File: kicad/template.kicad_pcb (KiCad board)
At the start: 2 copper layers, 84.1 x 61.7 mm, 7 parts, among them J1 Bus_PCI_Express_x1, J6 USB_C_Receptacle_USB2.0_16P, U1 MCP25625T-E/ML, U2 RP2040, U4 W25Q128JVP, X1 ABM8-272-T3, Y1 X322516MLB4SI

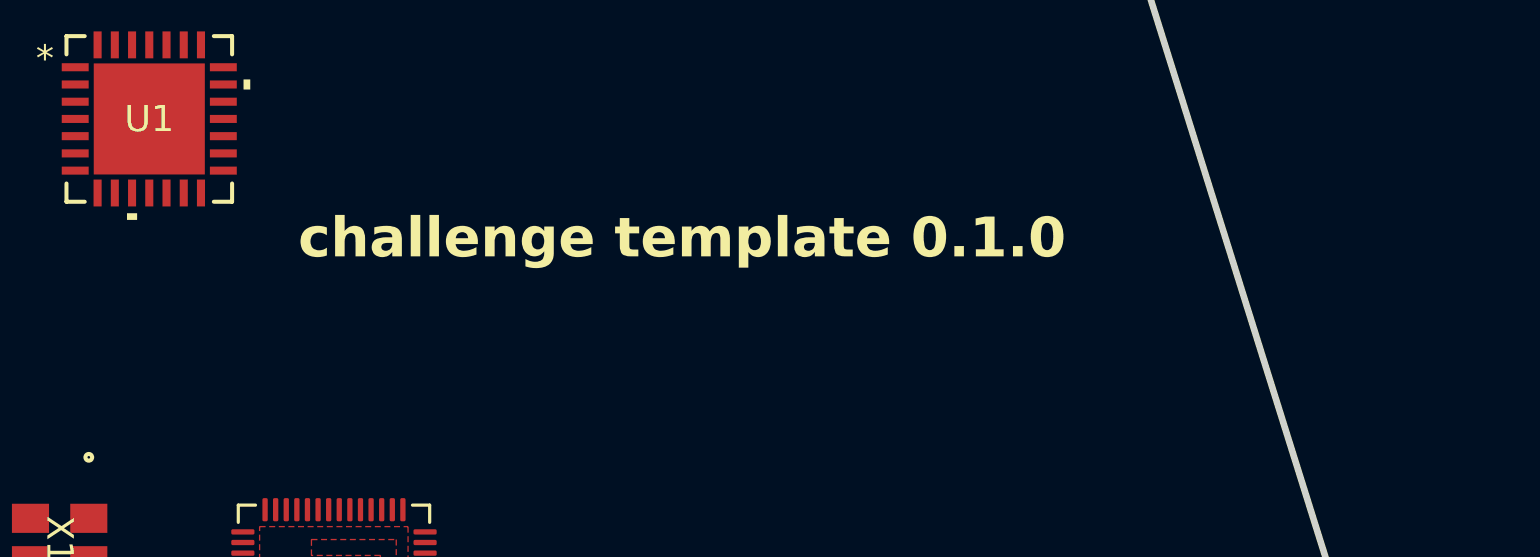
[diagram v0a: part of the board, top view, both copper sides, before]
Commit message: init status module
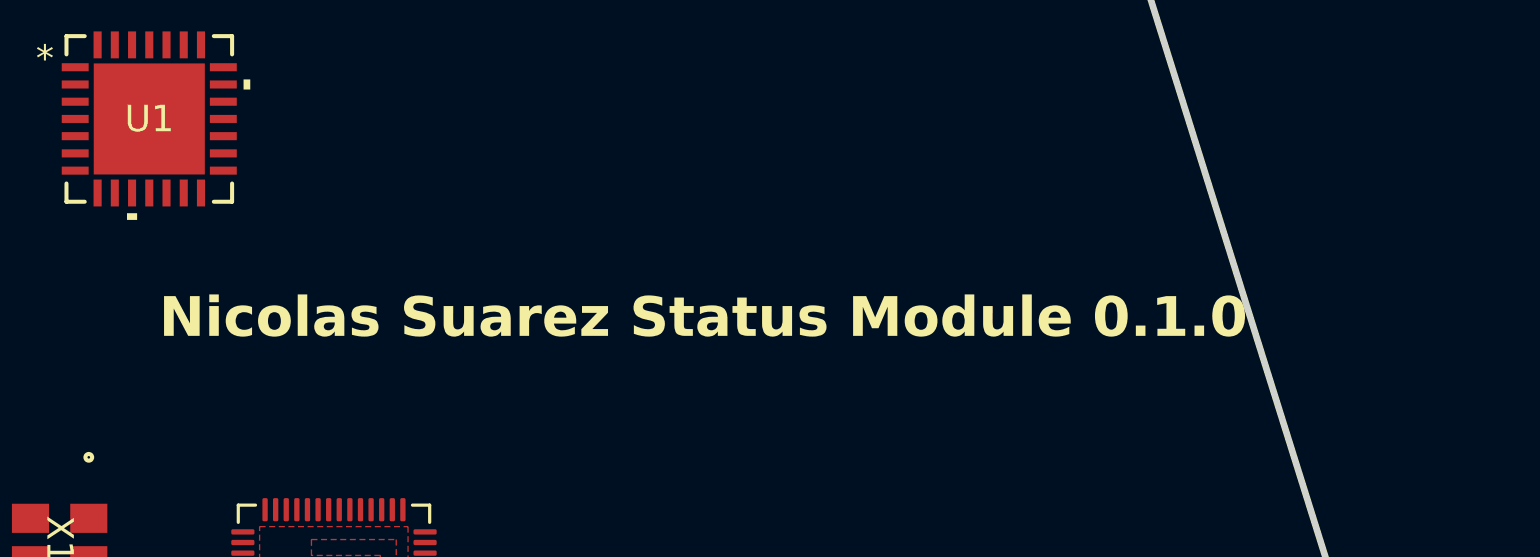
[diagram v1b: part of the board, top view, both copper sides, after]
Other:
- board text added: "Nicolas Suarez Status Module 0.1.0"
- board text removed: "challenge template 0.1.0"
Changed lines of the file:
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@@
 		(layer "Edge.Cuts")
 	)
-	(gr_text "challenge template 0.1.0"
-		(at 145.75 85.5 0)
+	(gr_text "Nicolas Suarez Status Module 0.1.0\n"
+		(at 140.5 88.5 0)
 		(layer "F.SilkS")
 		(effects

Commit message: Update schematic
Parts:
- added C1: 0.1 uF, Capacitor_SMD:C_0603_1608Metric, F.Cu at (159.1, 78.0)
- added C16: 100 nF, Capacitor_SMD:C_0603_1608Metric, F.Cu at (163.2, 80.5)
- added C17: 15 pF, Capacitor_SMD:C_0603_1608Metric, F.Cu at (163.2, 83.0)
- added C18: 15 pF, Capacitor_SMD:C_0603_1608Metric, F.Cu at (163.2, 85.5)
- added C19: 10 uF, Capacitor_SMD:C_0603_1608Metric, F.Cu at (162.0, 114.0)
- added C2: 0.1 uF, Capacitor_SMD:C_0603_1608Metric, F.Cu at (159.1, 80.5)
- added C20: 10 uF, Capacitor_SMD:C_0603_1608Metric, F.Cu at (163.2, 88.0)
- added C21: 100 nF, Capacitor_SMD:C_0603_1608Metric, F.Cu at (163.2, 90.5)
- added C22: 100 nF, Capacitor_SMD:C_0603_1608Metric, F.Cu at (137.2, 116.5)
- added C23: 100 nF, Capacitor_SMD:C_0603_1608Metric, F.Cu at (167.2, 78.0)
- added C24: 100 nF, Capacitor_SMD:C_0603_1608Metric, F.Cu at (167.2, 80.5)
- added C25: 100 nF, Capacitor_SMD:C_0603_1608Metric, F.Cu at (167.2, 83.0)
- added C26: 100 nF, Capacitor_SMD:C_0603_1608Metric, F.Cu at (167.2, 85.5)
- added C27: 100 nF, Capacitor_SMD:C_0603_1608Metric, F.Cu at (167.2, 88.0)
- added C3: 0.1 uF, Capacitor_SMD:C_0603_1608Metric, F.Cu at (159.1, 83.0)
- added C4: 0.22 uF, Capacitor_SMD:C_0603_1608Metric, F.Cu at (159.1, 85.5)
- added C5: 0.22 uF, Capacitor_SMD:C_0603_1608Metric, F.Cu at (159.1, 88.0)
- added C6: 1 uF, Capacitor_SMD:C_0603_1608Metric_Pad1.08x0.95mm_HandSolder, F.Cu at (143.5, 103.5)
- added C7: 100 nF, Capacitor_SMD:C_0603_1608Metric, F.Cu at (159.1, 90.5)
- added C8: 100 nF, Capacitor_SMD:C_0603_1608Metric, F.Cu at (159.1, 93.0)
- added C9: 1 uF, Capacitor_SMD:C_0603_1608Metric, F.Cu at (163.2, 78.0)
- added J2: Micro_SD_Card, Connector_Card:microSD_HC_Wuerth_693072010801, F.Cu at (123.6, 92.8)
- added J3: Conn_01x02_Pin, Connector_Hirose:Hirose_DF13-02P-1.25DSA_1x02_P1.25mm_Vertical, F.Cu at (131.4, 108.0)
- added R1: 120, Resistor_SMD:R_0603_1608Metric, F.Cu at (167.2, 90.5)
- added R2: 120, Resistor_SMD:R_0603_1608Metric, F.Cu at (141.2, 92.5)
- added R3: 1k, Resistor_SMD:R_0603_1608Metric, F.Cu at (171.2, 78.0)
- added R4: 27, Resistor_SMD:R_0603_1608Metric, F.Cu at (148.0, 103.5)
- added R5: 27, Resistor_SMD:R_0603_1608Metric, F.Cu at (148.5, 106.5)
- added R6: 1k, Resistor_SMD:R_0603_1608Metric, F.Cu at (171.2, 85.5)
- added R7: DNF, Resistor_SMD:R_0603_1608Metric, F.Cu at (171.2, 88.0)
- added U3: NCP1117-1.5_SOT223, Package_TO_SOT_SMD:SOT-223-3_TabPin2, F.Cu at (169.0, 112.0)
- turned U1 to 180 degrees
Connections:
- net Net-(J6-D+-PadA6) renamed /USB_P
- net Net-(J6-D--PadA7) renamed /USB_D
- J6 pad A4: unconnected-(J6-VBUS-PadA4)_1 -> VBUS
- J6 pad A9: unconnected-(J6-VBUS-PadA4) -> VBUS
- J6 pad B4: unconnected-(J6-VBUS-PadA4)_2 -> VBUS
- J6 pad B9: unconnected-(J6-VBUS-PadA4)_3 -> VBUS
- U1 pad 1: unconnected-(U1-*CS-Pad1) -> /CS
- U1 pad 10: unconnected-(U1-RXD-Pad10) -> /RX
- U1 pad 11: unconnected-(U1-VIO-Pad11) -> +3.3V
- U1 pad 12: unconnected-(U1-CANL-Pad12) -> CANN
- U1 pad 13: unconnected-(U1-CANH-Pad13) -> CANP
- U1 pad 15: unconnected-(U1-STBY-Pad15) -> /STBY
- U1 pad 16: unconnected-(U1-TXD-Pad16) -> /TX
- U1 pad 18: unconnected-(U1-VSS-Pad18) -> GND
- U1 pad 19: unconnected-(U1-VDDA-Pad19) -> +5V
- U1 pad 2: unconnected-(U1-*RESET-Pad2) -> /RESET
- U1 pad 20: unconnected-(U1-OSC2-Pad20) -> /OSC2
- U1 pad 21: unconnected-(U1-OSC1-Pad21) -> /OSC1
- U1 pad 22: unconnected-(U1-GND-Pad22) -> GND
- U1 pad 26: unconnected-(U1-SCK-Pad26) -> /SCK
- U1 pad 27: unconnected-(U1-SI-Pad27) -> /MOSI
- U1 pad 28: unconnected-(U1-SO-Pad28) -> /MISO
- U1 pad 3: unconnected-(U1-VDD-Pad3) -> +3.3V
- U1 pad 4: unconnected-(U1-TXCAN-Pad4) -> /TX
- U1 pad 5: unconnected-(U1-RXCAN-Pad5) -> /RX
- U2 pad 1: Net-(U2-IOVDD-Pad1) -> +3.3V
- U2 pad 10: Net-(U2-IOVDD-Pad1) -> +3.3V
- U2 pad 16: unconnected-(U2-GPIO13-Pad16) -> /CS_SD
- U2 pad 19: unconnected-(U2-TESTEN-Pad19) -> GND
- U2 pad 2: unconnected-(U2-GPIO0-Pad2) -> /STBY
- U2 pad 20: unconnected-(U2-XIN-Pad20) -> /X_IN
- U2 pad 21: unconnected-(U2-XOUT-Pad21) -> /X_OUT
- U2 pad 22: Net-(U2-IOVDD-Pad1) -> +3.3V
- U2 pad 23: Net-(U2-DVDD-Pad23) -> +1V1
- U2 pad 28: unconnected-(U2-GPIO17-Pad28) -> /CS
- U2 pad 29: unconnected-(U2-GPIO18-Pad29) -> /SCK
- U2 pad 33: Net-(U2-IOVDD-Pad1) -> +3.3V
- U2 pad 42: Net-(U2-IOVDD-Pad1) -> +3.3V
- U2 pad 43: unconnected-(U2-ADC_AVDD-Pad43) -> +3.3V
- U2 pad 44: unconnected-(U2-VREG_IN-Pad44) -> +3.3V
- U2 pad 45: unconnected-(U2-VREG_VOUT-Pad45) -> +1V1
- U2 pad 46: unconnected-(U2-USB_DM-Pad46) -> Net-(U2-USB_DM)
- U2 pad 47: unconnected-(U2-USB_DP-Pad47) -> Net-(U2-USB_DP)
- U2 pad 48: unconnected-(U2-USB_VDD-Pad48) -> +3.3V
- U2 pad 49: Net-(U2-IOVDD-Pad1) -> +3.3V
- U2 pad 5: unconnected-(U2-GPIO3-Pad5) -> /MOSI
- U2 pad 50: Net-(U2-DVDD-Pad23) -> +1V1
- U2 pad 51: unconnected-(U2-QSPI_SD3-Pad51) -> /QSPI_SD3
- U2 pad 52: unconnected-(U2-QSPI_SCLK-Pad52) -> /QSPI_CLK
- U2 pad 53: unconnected-(U2-QSPI_SD0-Pad53) -> /QSPI_SD0
- U2 pad 54: unconnected-(U2-QSPI_SD2-Pad54) -> /QSPI_SD2
- U2 pad 55: unconnected-(U2-QSPI_SD1-Pad55) -> /QSPI_SD1
- U2 pad 56: unconnected-(U2-QSPI_SS-Pad56) -> /QSPI_SS
- U2 pad 57: unconnected-(U2-GND-Pad57) -> GND
- U2 pad 6: unconnected-(U2-GPIO4-Pad6) -> /MISO
- U2 pad 9: unconnected-(U2-GPIO7-Pad9) -> /RESET
- U4 pad 1: unconnected-(U4-~{CS}-Pad1) -> /QSPI_SS
- U4 pad 2: unconnected-(U4-DO(IO1)-Pad2) -> /QSPI_SD1
- U4 pad 3: unconnected-(U4-IO2-Pad3) -> /QSPI_SD2
- U4 pad 4: unconnected-(U4-GND-Pad4) -> GND
- U4 pad 5: unconnected-(U4-DI(IO0)-Pad5) -> /QSPI_SD0
- U4 pad 6: unconnected-(U4-CLK-Pad6) -> /QSPI_CLK
- U4 pad 7: unconnected-(U4-IO3-Pad7) -> /QSPI_SD3
- U4 pad 8: unconnected-(U4-VCC-Pad8) -> +3.3V
- X1 pad 1: unconnected-(X1-Pad1) -> /X_IN
- X1 pad 2: unconnected-(X1-Pad2) -> GND
- X1 pad 3: unconnected-(X1-Pad3) -> Net-(C18-Pad1)
- X1 pad 4: unconnected-(X1-Pad4) -> GND
- Y1 pad 1: unconnected-(Y1-Pad1) -> /OSC1
- Y1 pad 2: Net-(Y1-Pad2) -> GND
- Y1 pad 3: unconnected-(Y1-Pad3) -> /OSC2
- Y1 pad 4: Net-(Y1-Pad2) -> GND
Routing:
- added copper zone on F.Cu, net +1V1
- removed copper zone on F.Cu, net unconnected-(U2-VREG_VOUT-Pad45)

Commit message: update schematic and pcb layout
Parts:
- removed C20: 10 uF, Capacitor_SMD:C_0603_1608Metric
- removed R1, R2: 120, Resistor_SMD:R_0603_1608Metric
- removed U3: NCP1117-1.5_SOT223, Package_TO_SOT_SMD:SOT-223-3_TabPin2
- moved J3 40.8 mm to (171.2, 116.5)
- moved R3 40.1 mm to (138.0, 100.5), turned to 90 degrees
- moved R6 31.9 mm to (163.5, 116.5)
- moved C18 31.4 mm to (135.5, 100.3), turned to -90 degrees
- moved C22 28.0 mm to (156.0, 95.7), turned to 180 degrees
- moved C9 27.7 mm to (156.0, 104.8), turned to 180 degrees
- moved C17 26.8 mm to (137.9, 92.0), turned to 90 degrees
- moved C4 25.4 mm to (134.2, 80.7)
- moved C3 25.4 mm to (134.2, 78.0)
- moved C5 25.3 mm to (134.3, 83.3)
- moved R7 23.6 mm to (173.8, 111.4), turned to 180 degrees
- moved C23 22.2 mm to (156.0, 97.2), turned to 180 degrees
- moved C24 21.4 mm to (156.0, 98.7), turned to 180 degrees
- moved C7 21.3 mm to (143.0, 104.5), turned to -90 degrees
- moved C8 21.3 mm to (141.0, 104.3), turned to -90 degrees
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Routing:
- net /MISO: track 0.00 -> 67.9 mm, vias 0 -> 3
- net /MOSI: track 0.00 -> 55.3 mm, vias 0 -> 3
- net +5V: track 0.00 -> 32.3 mm, vias 0 -> 2
- net /SCK: track 0.00 -> 25.8 mm
- net /OSC1: track 0.00 -> 20.3 mm
- net +3.3V: track 0.00 -> 17.8 mm
- net /X_OUT: track 0.00 -> 16.6 mm, vias 0 -> 2
- net CANP: track 0.00 -> 14.0 mm
- net CANN: track 0.00 -> 13.5 mm
- net /OSC2: track 0.00 -> 12.7 mm
- net /USB_P: track 0.00 -> 9.32 mm
- net /RX: track 0.00 -> 9.31 mm, vias 0 -> 2
- net /USB_D: track 0.00 -> 9.19 mm
- net Net-(U2-USB_DP): track 0.00 -> 3.27 mm
- net Net-(C18-Pad1): track 0.00 -> 2.76 mm
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
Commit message: update BOM
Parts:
- removed R7: DNF, Resistor_SMD:R_0603_1608Metric
- C6: footprint Capacitor_SMD:C_0603_1608Metric_Pad1.08x0.95mm_HandSolder -> Capacitor_SMD:C_0603_1608Metric
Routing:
- net /QSPI_SS: track 2.33 -> 0.06 mm

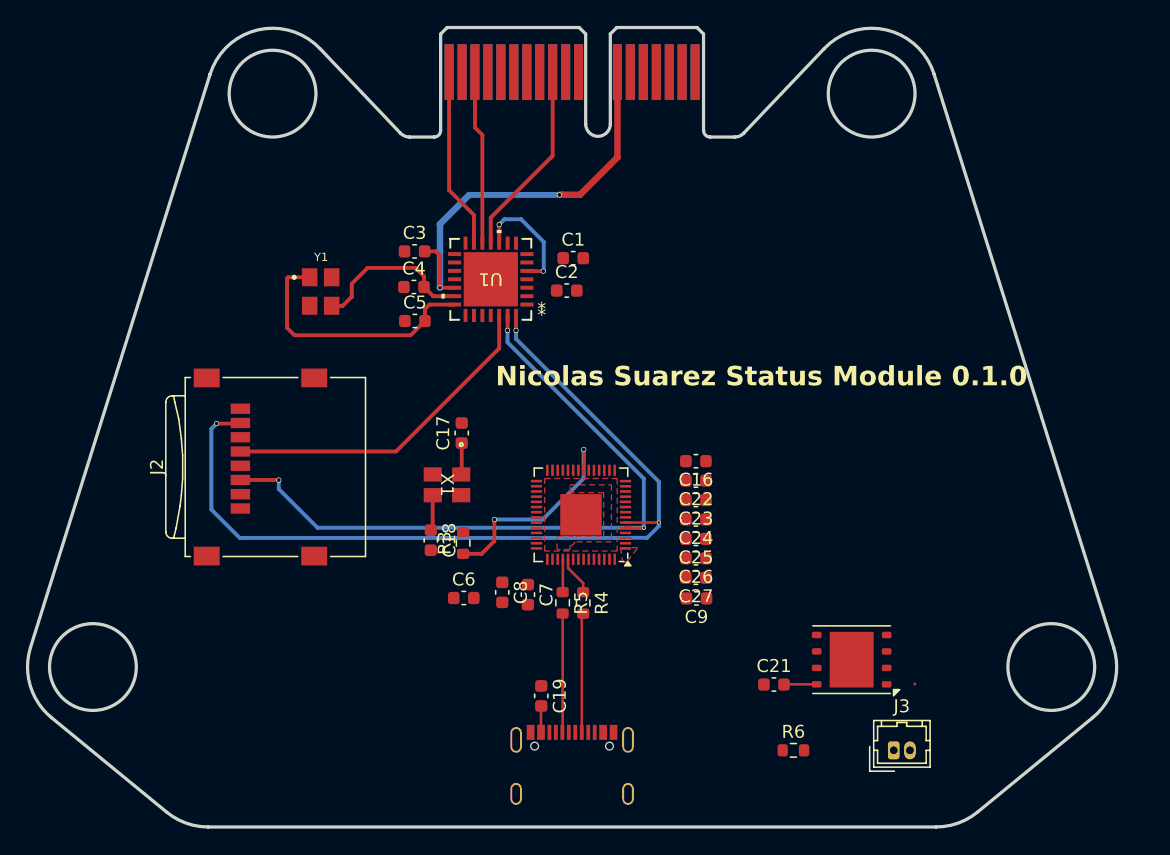
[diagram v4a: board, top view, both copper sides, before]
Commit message: update schematic
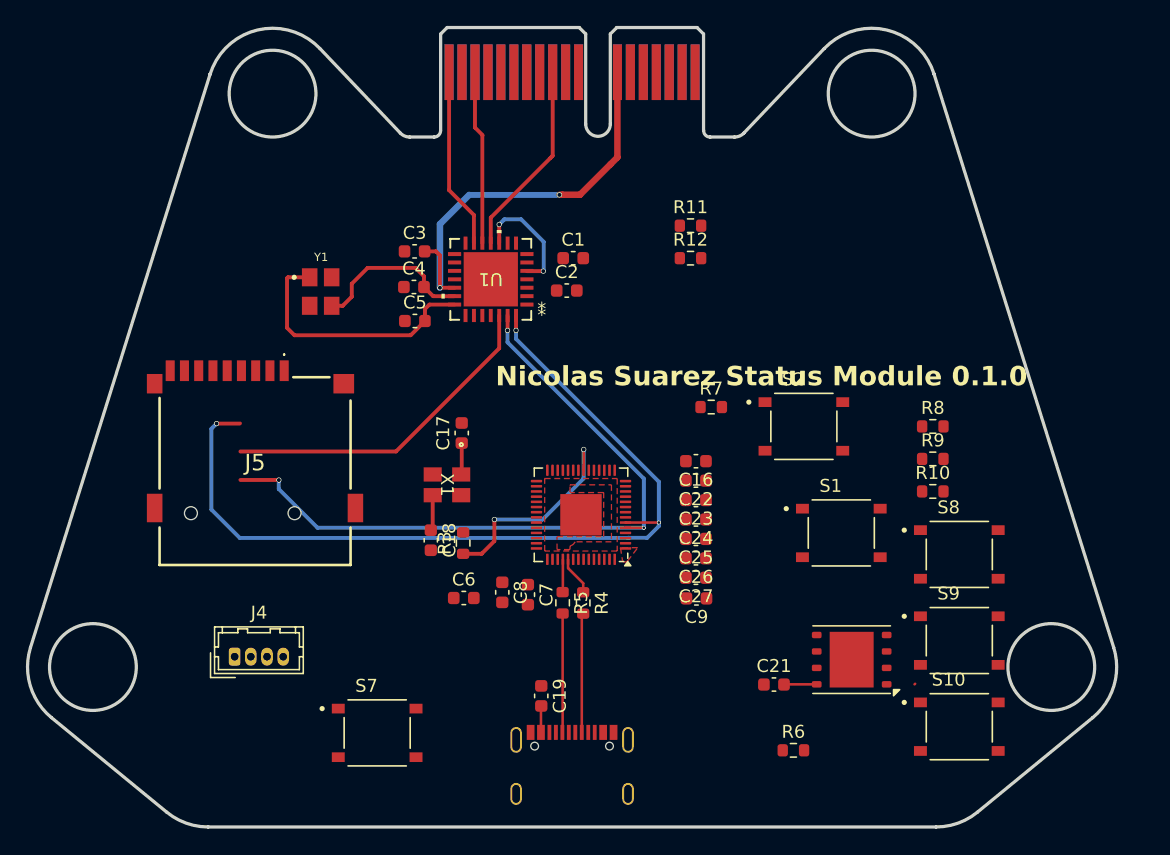
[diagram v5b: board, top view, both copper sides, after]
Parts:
- removed J2: Micro_SD_Card, Connector_Card:microSD_HC_Wuerth_693072010801
- removed J3: Conn_01x02_Pin, Connector_Hirose:Hirose_DF13-02P-1.25DSA_1x02_P1.25mm_Vertical
- added J4: Conn_01x04_Socket, Connector_Hirose:Hirose_DF13-04P-1.25DSA_1x04_P1.25mm_Vertical, F.Cu at (120.4, 109.3)
- added J5: TF-115-BCP9, Nicolas Library:TF115BCP9, F.Cu at (121.9, 94.9)
- added R10: 10K, Resistor_SMD:R_0603_1608Metric, F.Cu at (174.3, 96.5)
- added R11: 5.1K, Resistor_SMD:R_0603_1608Metric, F.Cu at (155.6, 76.0)
- added R12: 5.1K, Resistor_SMD:R_0603_1608Metric, F.Cu at (155.6, 78.5)
- added R7: 10K, Resistor_SMD:R_0603_1608Metric, F.Cu at (157.2, 90.0)
- added R8: 10K, Resistor_SMD:R_0603_1608Metric, F.Cu at (174.3, 91.5)
- added R9: 10K, Resistor_SMD:R_0603_1608Metric, F.Cu at (174.3, 94.0)
- added S1: TS-1187A-B-A-B, Nicolas Library:SW_TS-1187A-B-A-B, F.Cu at (167.2, 99.7)
- added S10: TS-1187A-B-A-B, Nicolas Library:SW_TS-1187A-B-A-B, F.Cu at (176.3, 114.7)
- added S2: TS-1187A-B-A-B, Nicolas Library:SW_TS-1187A-B-A-B, F.Cu at (164.3, 91.5)
- added S7: TS-1187A-B-A-B, Nicolas Library:SW_TS-1187A-B-A-B, F.Cu at (131.4, 115.2)
- added S8: TS-1187A-B-A-B, Nicolas Library:SW_TS-1187A-B-A-B, F.Cu at (176.3, 101.4)
- added S9: TS-1187A-B-A-B, Nicolas Library:SW_TS-1187A-B-A-B, F.Cu at (176.3, 108.0)
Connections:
- R6 pad 2: Net-(J3-Pin_1) -> /~{USB_BOOT_S}
- U2 pad 11: unconnected-(U2-GPIO8-Pad11) -> /Push_B1
- U2 pad 13: unconnected-(U2-GPIO10-Pad13) -> /SDA
- U2 pad 14: unconnected-(U2-GPIO11-Pad14) -> /SCL
- U2 pad 26: unconnected-(U2-RUN-Pad26) -> Net-(U2-RUN)
- U2 pad 30: unconnected-(U2-GPIO19-Pad30) -> /Push_B1
- U2 pad 31: unconnected-(U2-GPIO20-Pad31) -> /Push_B2
- U2 pad 35: unconnected-(U2-GPIO23-Pad35) -> /Push_B3
- U2 pad 36: unconnected-(U2-GPIO24-Pad36) -> /Push_B4

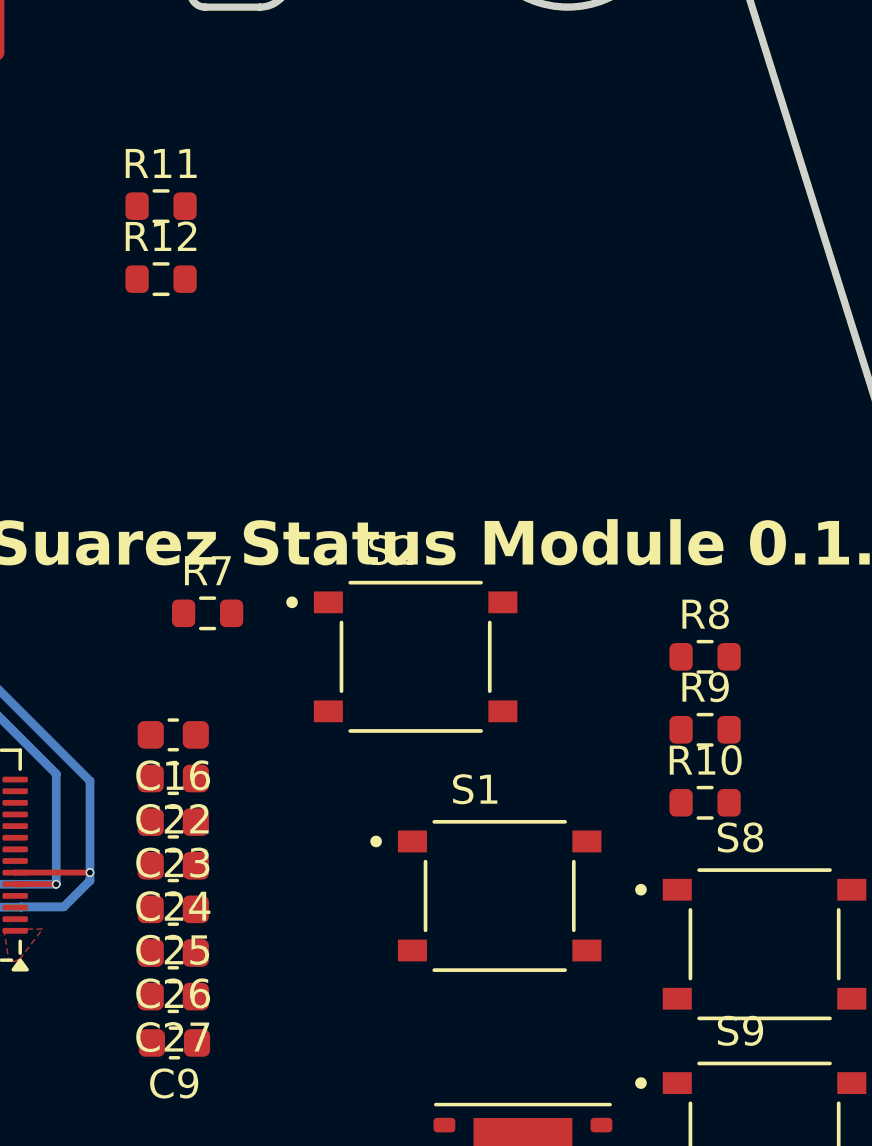
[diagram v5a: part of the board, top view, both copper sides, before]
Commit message: update schematic
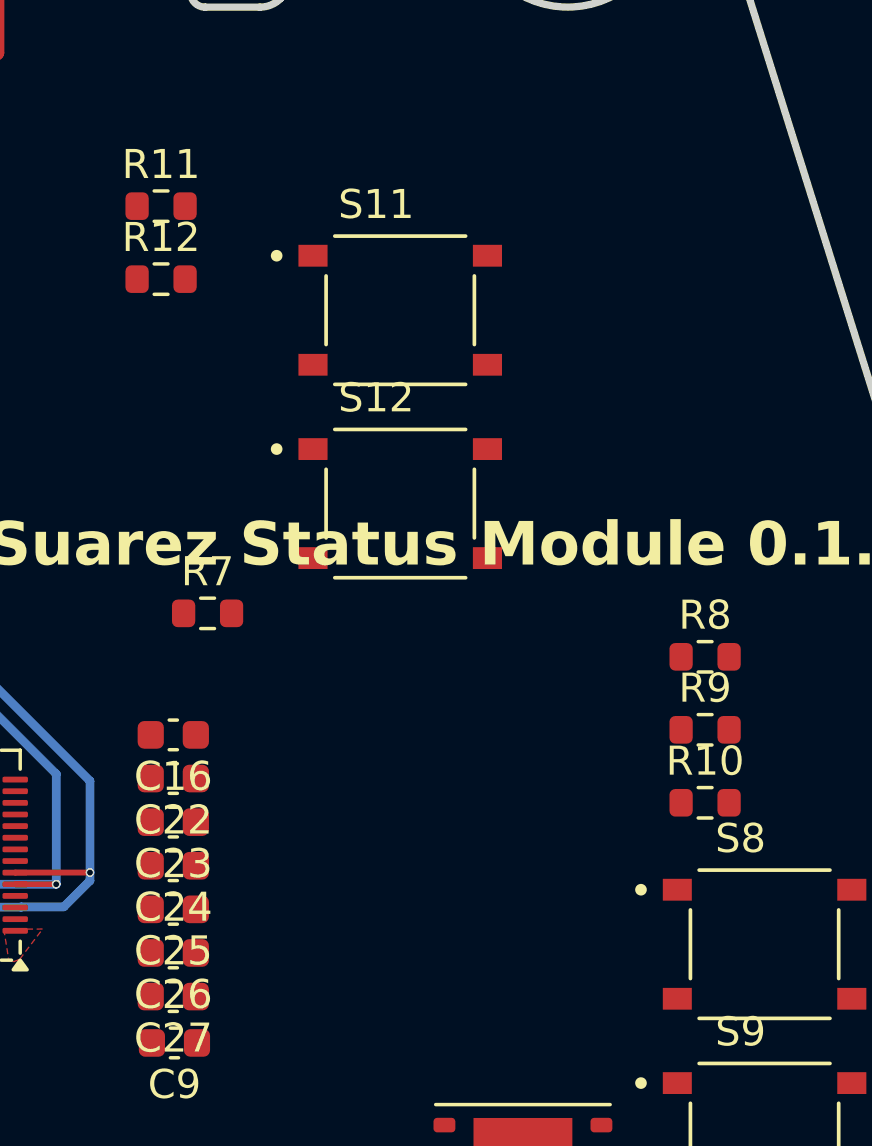
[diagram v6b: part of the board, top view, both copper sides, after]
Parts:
- removed S1, S2: TS-1187A-B-A-B, Nicolas Library:SW_TS-1187A-B-A-B
- added S11: TS-1187A-B-A-B, Nicolas Library:SW_TS-1187A-B-A-B, F.Cu at (163.8, 79.6)
- added S12: TS-1187A-B-A-B, Nicolas Library:SW_TS-1187A-B-A-B, F.Cu at (163.8, 86.2)
